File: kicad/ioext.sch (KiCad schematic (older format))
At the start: 46 parts, among them P1 CONN_01X04, P2 CONN_02X08, P3 CONN_01X10, Q1 IRLZ44N, Q2 IRLZ44N, Q3 IRLZ44N, Q4 IRLZ44N, Q5 IRLZ44N, Q6 IRLZ44N, Q7 IRLZ44N, Q8 IRLZ44N, U1 PCF8574A, U2 PC817, U3 PC817, U4 PC817, U5 PC817, U6 PC817, U7 PC817, U8 PC817, U9 PC817

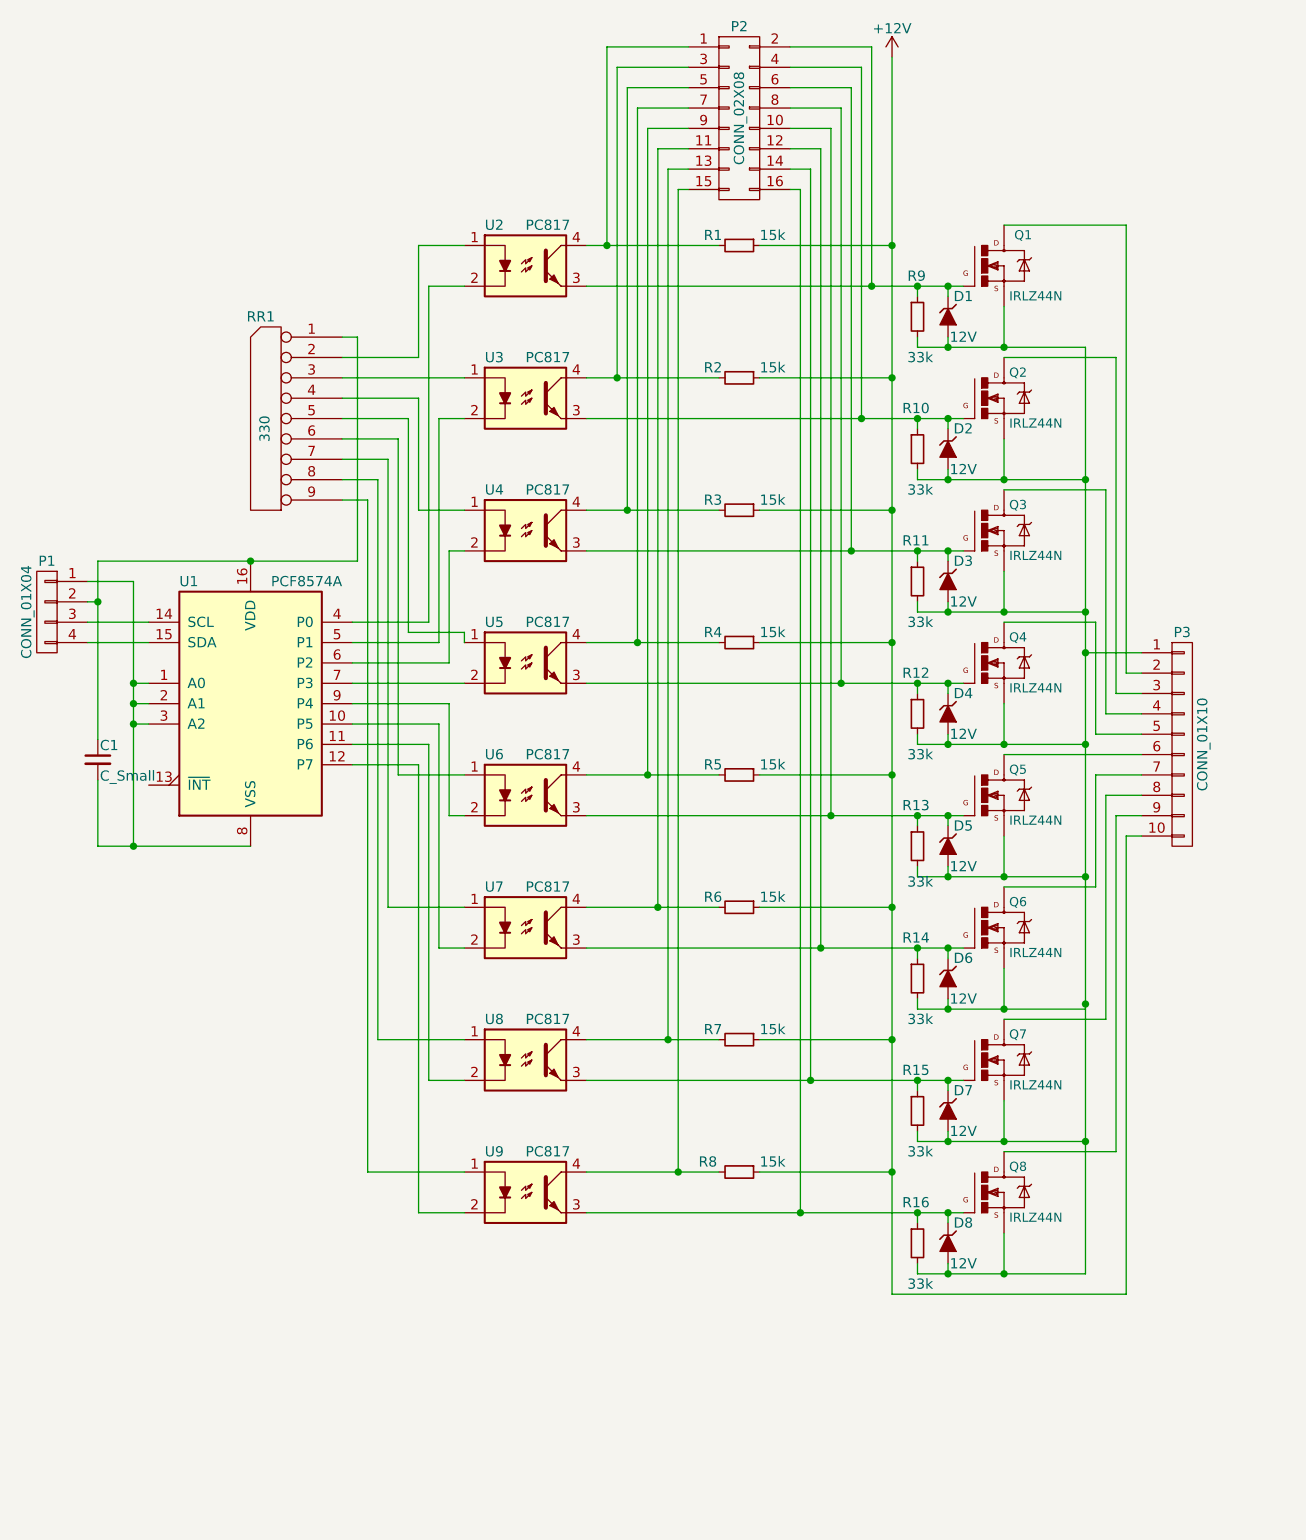
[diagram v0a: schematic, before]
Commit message: kicad-ioext: components distributed
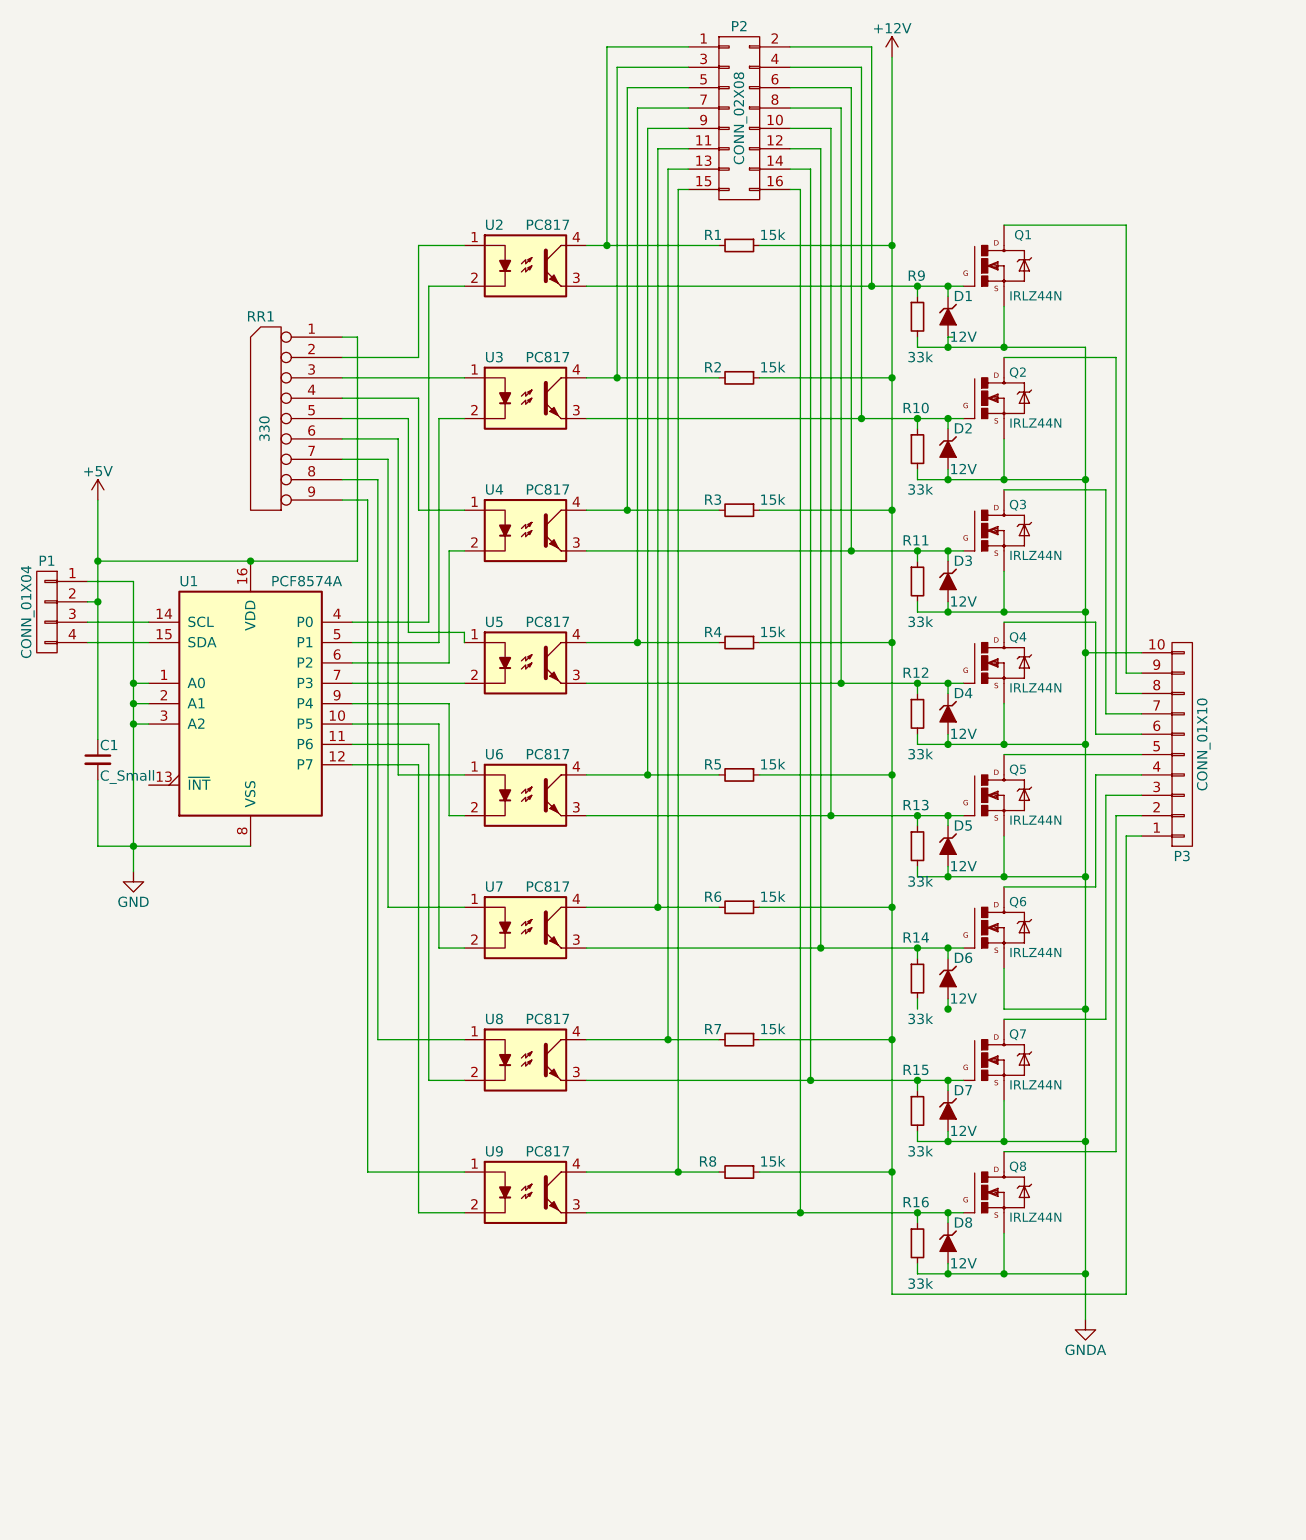
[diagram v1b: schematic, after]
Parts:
- P2: footprint gate433:Pin_Header_Straight_2x08 -> Pin_Headers:Pin_Header_Straight_2x08
- RR1: footprint Resistors_ThroughHole:Resistor_Array_SIP9 -> Resistors_ThroughHole:Resistor_Array_SIP8
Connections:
- net +12V: now also P3.1 (P1); no longer P3.10 (P10)
- net GNDA: now reaches D1.2 (A), D2.2 (A), D3.2 (A), D4.2 (A), D5.2 (A), D7.2 (A), D8.2 (A), Q1.3 (S), Q2.3 (S), Q3.3 (S), Q4.3 (S), Q5.3 (S), Q7.3 (S), Q8.3 (S), R10.2, R11.2, R12.2, R13.2, R15.2, R16.2, R9.2
- net GNDA: now also P3.10 (P10), Q6.3 (S); no longer P3.1 (P1)
- net at P3.2 (P2): now also Q8.2 (D); no longer Q1.2 (D)
- net at P3.3 (P3): now also Q7.2 (D); no longer Q2.2 (D)
- net at P3.4 (P4): now also Q6.2 (D); no longer Q3.2 (D)
- net at P3.5 (P5): now also Q5.2 (D); no longer Q4.2 (D)
- net at P3.6 (P6): now also Q4.2 (D); no longer Q5.2 (D)
- net at P3.7 (P7): now also Q3.2 (D); no longer Q6.2 (D)
- net at P3.8 (P8): now also Q2.2 (D); no longer Q7.2 (D)
- net at P3.9 (P9): now also Q1.2 (D); no longer Q8.2 (D)
- net +5V: now reaches C1.1, P1.2 (P2), RR1.1 (COM), U1.16 (VDD)
- net GND: now reaches C1.2, P1.1 (P1), U1.1 (A0), U1.2 (A1), U1.3 (A2), U1.8 (VSS)
- now unconnected: D6.2 (A), R14.2

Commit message: kicad-ioext: wiring
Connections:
- net GNDA: now also D6.2 (A), R14.2; no longer Q6.3 (S)
- net at P1.3 (P3): now also U1.15 (SDA); no longer U1.14 (SCL)
- net at P1.4 (P4): now also U1.14 (SCL); no longer U1.15 (SDA)
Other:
- moved on the sheet: C1, D1, D2, D3, D4, D5, D6, D7, D8, P1, P2, P3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
